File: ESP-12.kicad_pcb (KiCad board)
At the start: 2 copper layers, 27 x 38.2 mm, 23 parts, among them P1 VCC, P2 GPIO_1, P3 SPI, P4 GPIO_2, P5 GND, SW1 FLASH, SW2 RESET, U1 ESP-12E, U2 AP1117-33

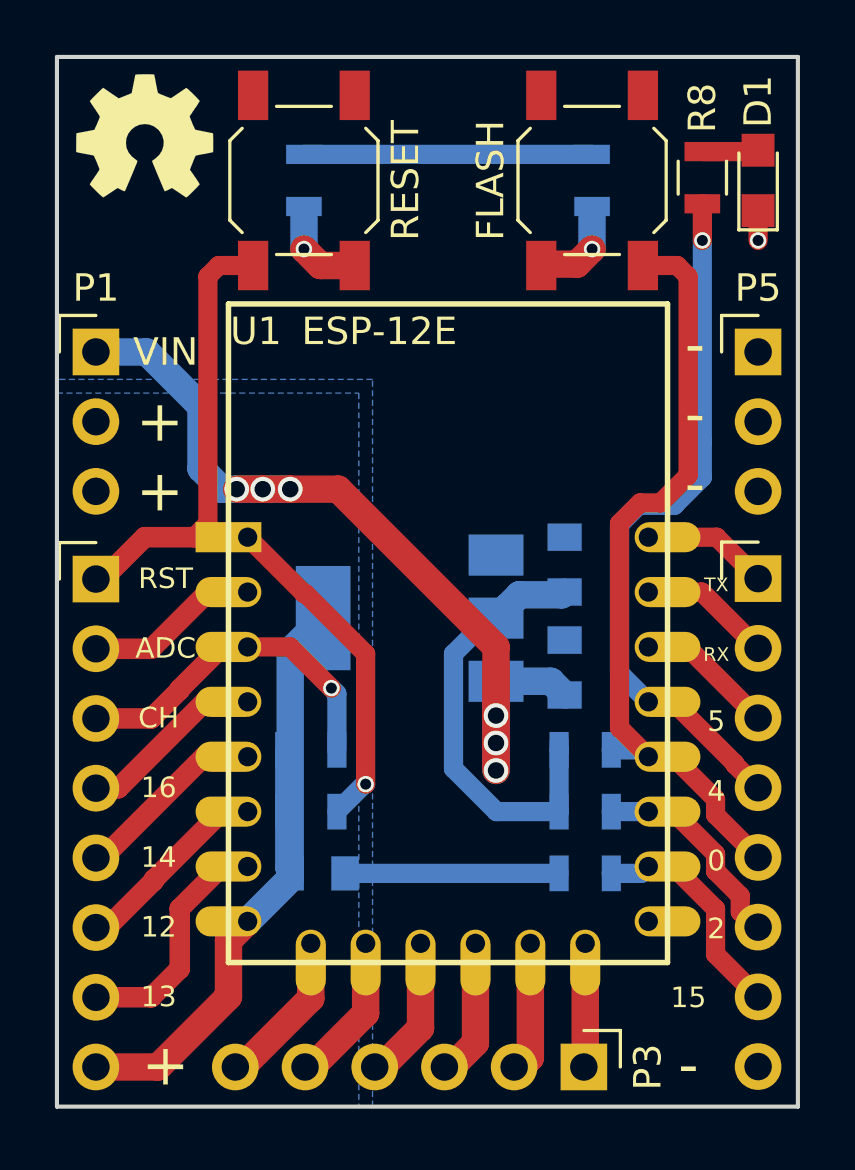
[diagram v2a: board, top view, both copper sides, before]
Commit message: Adjust pitch of power headers to match other headers
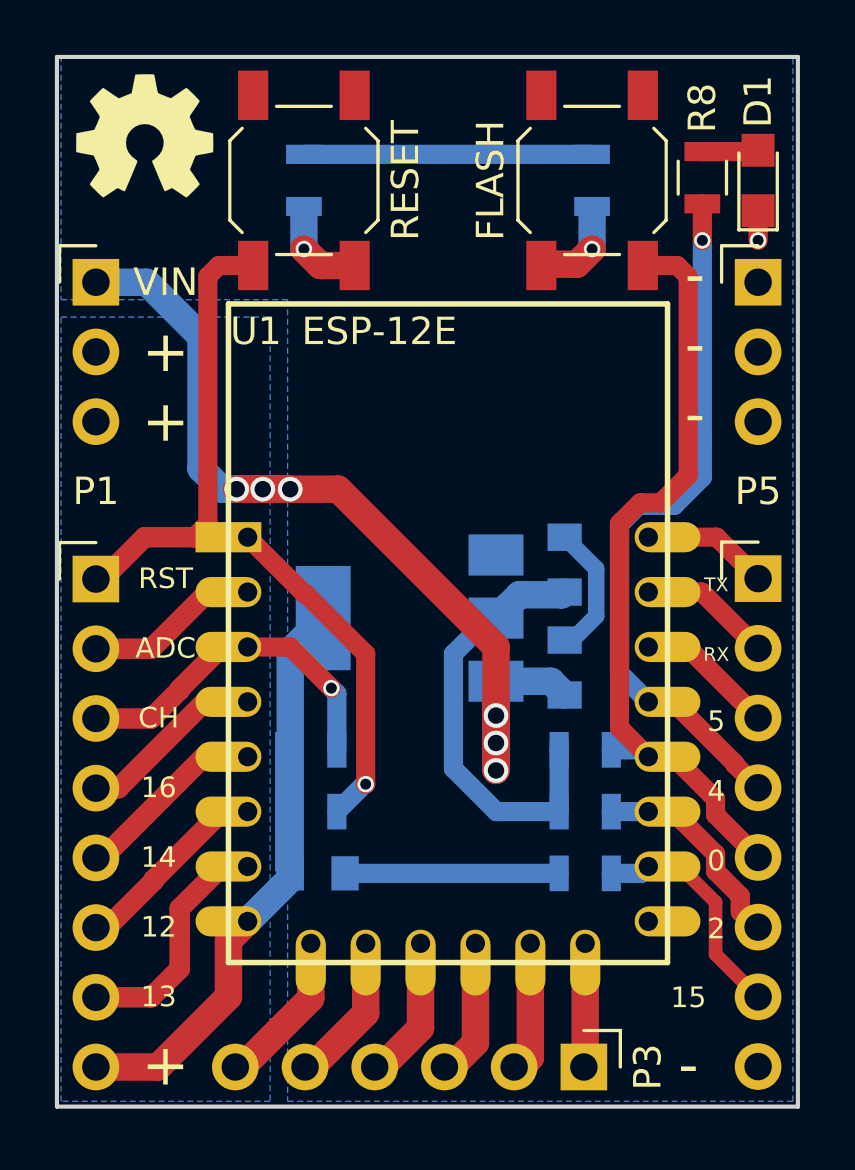
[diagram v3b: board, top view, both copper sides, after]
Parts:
- moved P1 2.54 mm to (27.4, 42.0)
- moved P5 2.54 mm to (51.5, 42.0)
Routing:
- net GND: track 19.6 -> 24.6 mm
- net /VIN: track 33.0 -> 35.3 mm
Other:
- board text added: "www.falseascension.xyz github.com/FalseAscension/"
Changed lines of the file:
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@@
   (general
     (links 60)
-    (no_connects 8)
-    (area 25.924999 33.674999 53.075001 72.075001)
+    (no_connects 7)
+    (area 14.150001 13.65 190.885715 164.950001)
     (thickness 1.6)
-    (drawings 61)
-    (tracks 162)
+    (drawings 62)
+    (tracks 168)
     (zones 0)
     (modules 23)
@@
   )
   (setup
-    (last_trace_width 0.7)
+    (last_trace_width 0.6)
     (user_trace_width 0.2)
     (user_trace_width 0.25)
@@
     (model /home/emil/Circuits/Library/kicad-ESP8266/ESP8266.3dshapes/ESP-12.wrl
       (at (xyz 0.025 0 0))
-      (scale (xyz 0.41 0.39 0.42))
+      (scale (xyz 0.41 0.395 0.42))
       (rotate (xyz 0 0 0))
     )
@@
   )
   (module Misc_Footprints:Pin_Header_Straight_1x03_Pitch2.54mm (layer F.Cu)
-    (at 51.55 44.5)
+    (at 51.55 41.96)
     (descr "Through hole straight pin header, 1x03, 2.54mm pitch, single row")
     (tags "Through hole pin header THT 1x03 2.54mm single row")
-    (fp_text reference P5 (at 0 -2.33) (layer F.SilkS)
-      (effects (font (size 1 1) (thickness 0.15)))
-    )
-    (fp_text value GND (at -0.05 -2.25) (layer F.Fab)
+    (fp_text reference P5 (at 0 7.62) (layer F.SilkS)
+      (effects (font (size 1 1) (thickness 0.15)))
+    )
+    (fp_text value GND (at 0 7.62) (layer F.Fab)
       (effects (font (size 1 1) (thickness 0.15)))
     )
@@
   )
   (module Misc_Footprints:Pin_Header_Straight_1x03_Pitch2.54mm (layer F.Cu)
-    (at 27.42 44.5)
+    (at 27.42 41.96)
     (descr "Through hole straight pin header, 1x03, 2.54mm pitch, single row")
     (tags "Through hole pin header THT 1x03 2.54mm single row")
-    (fp_text reference P1 (at 0 -2.33) (layer F.SilkS)
-      (effects (font (size 1 1) (thickness 0.15)))
-    )
-    (fp_text value VCC (at -0.05 -2.25) (layer F.Fab)
+    (fp_text reference P1 (at 0 7.62) (layer F.SilkS)
+      (effects (font (size 1 1) (thickness 0.15)))
+    )
+    (fp_text value VCC (at -0.05 7.62) (layer F.Fab)
       (effects (font (size 1 1) (thickness 0.15)))
     )
@@
       (effects (font (size 0.13462 0.13462) (thickness 0.0254)) (justify mirror))
     )
-    (fp_text user github.com/FalseAscension (at 7.578 -0.114 180) (layer B.SilkS)
+    (fp_text user github.com/FalseAscension (at 7.578 -0.114 180) (layer B.SilkS) hide
       (effects (font (size 0.8 0.8) (thickness 0.125)) (justify mirror))
     )
-    (fp_text user www.falseascension.xyz (at 7.324 1.156 180) (layer B.SilkS)
+    (fp_text user www.falseascension.xyz (at 7.324 1.156 180) (layer B.SilkS) hide
       (effects (font (size 1 1) (thickness 0.125)) (justify mirror))
     )
@@
       (xy -1.51384 2.24536)) (layer F.SilkS) (width 0.00254))
   )
+  (gr_text "www.falseascension.xyz\ngithub.com/FalseAscension/" (at 44.438 35.356) (layer B.SilkS)
+    (effects (font (size 0.75 0.75) (thickness 0.15)) (justify mirror))
+  )
   (gr_text "2\n\n\n" (at 50.026 66.725) (layer F.SilkS)
     (effects (font (size 0.75 0.75) (thickness 0.15)))
@@
     (effects (font (size 1.5 1.5) (thickness 0.3)) (justify mirror))
   )
-  (gr_text "12\n" (at 29.706 65.328 360) (layer B.SilkS)
+  (gr_text "12\n" (at 29.706 65.328) (layer B.SilkS)
     (effects (font (size 0.75 0.75) (thickness 0.15)) (justify mirror))
   )
-  (gr_text 14 (at 29.706 62.915 360) (layer B.SilkS)
+  (gr_text 14 (at 29.706 62.915) (layer B.SilkS)
     (effects (font (size 0.75 0.75) (thickness 0.15)) (justify mirror))
   )
-  (gr_text 16 (at 29.706 60.375 360) (layer B.SilkS)
+  (gr_text 16 (at 29.706 60.375) (layer B.SilkS)
     (effects (font (size 0.75 0.75) (thickness 0.15)) (justify mirror))
   )
-  (gr_text "CH\n" (at 29.706 57.962 360) (layer B.SilkS)
+  (gr_text "CH\n" (at 29.706 57.962) (layer B.SilkS)
     (effects (font (size 0.75 0.75) (thickness 0.15)) (justify mirror))
   )
-  (gr_text ADC (at 29.951708 55.295 360) (layer B.SilkS)
+  (gr_text ADC (at 29.951708 55.295) (layer B.SilkS)
     (effects (font (size 0.75 0.75) (thickness 0.15)) (justify mirror))
   )
-  (gr_text RST (at 29.951708 52.755 360) (layer B.SilkS)
+  (gr_text RST (at 29.951708 52.755) (layer B.SilkS)
     (effects (font (size 0.75 0.75) (thickness 0.15)) (justify mirror))
   )
-  (gr_text "13\n" (at 29.706 67.995 360) (layer B.SilkS)
+  (gr_text "13\n" (at 29.706 67.995) (layer B.SilkS)
     (effects (font (size 0.75 0.75) (thickness 0.15)) (justify mirror))
   )
@@
     (effects (font (size 1.5 1.5) (thickness 0.3)))
   )
-  (gr_text - (at 49.25 49.58 180) (layer F.SilkS)
+  (gr_text - (at 49.25 41.96 180) (layer F.SilkS)
     (effects (font (size 1.5 1.5) (thickness 0.3)))
   )
-  (gr_text "VIN\n" (at 29.96 44.5) (layer F.SilkS)
+  (gr_text "VIN\n" (at 29.96 41.96) (layer F.SilkS)
     (effects (font (size 1 1) (thickness 0.2)))
   )
-  (gr_text + (at 29.75 47.04) (layer F.SilkS)
+  (gr_text + (at 29.96 44.5) (layer F.SilkS)
     (effects (font (size 1.5 1.5) (thickness 0.3)))
   )
-  (gr_text + (at 29.75 49.58) (layer F.SilkS)
+  (gr_text + (at 29.96 47.04) (layer F.SilkS)
     (effects (font (size 1.5 1.5) (thickness 0.3)))
   )
@@
     (effects (font (size 1.5 1.5) (thickness 0.3)))
   )
+  (segment (start 44.5 51.25) (end 45.64998 52.39998) (width 0.6) (layer B.Cu) (net 1))
+  (segment (start 45.64998 52.39998) (end 45.64998 54.125022) (width 0.6) (layer B.Cu) (net 1))
+  (segment (start 45.64998 54.125022) (end 44.775002 55) (width 0.6) (layer B.Cu) (net 1))
+  (segment (start 44.775002 55) (end 44.5 55) (width 0.6) (layer B.Cu) (net 1))
+  (segment (start 44.5 55) (end 44.625 55) (width 0.25) (layer B.Cu) (net 1))
   (segment (start 45.5 37.3) (end 35 37.3) (width 0.7) (layer B.Cu) (net 1))
   (segment (start 51.55 39.35) (end 51.55 40.436) (width 0.7) (layer F.Cu) (net 1))
@@
   (segment (start 27.67 70.556) (end 29.686 70.556) (width 1) (layer F.Cu) (net 2))
   (segment (start 29.686 70.556) (end 32.25 67.992) (width 1) (layer F.Cu) (net 2))
+  (segment (start 27.42 44.5) (end 27.42 44.745998) (width 1) (layer B.Cu) (net 2))
   (segment (start 32.95 53.25) (end 31.502 53.25) (width 0.75) (layer F.Cu) (net 3))
   (segment (start 31.502 53.25) (end 29.436 55.316) (width 0.75) (layer F.Cu) (net 3))
@@
   (segment (start 35.25 66.25) (end 35.25 68.056) (width 1) (layer F.Cu) (net 19))
   (segment (start 35.25 68.056) (end 32.75 70.556) (width 1) (layer F.Cu) (net 19))
+  (segment (start 50 64.551375) (end 50 66.45) (width 0.5) (layer F.Cu) (net 20))
+  (segment (start 50 66.45) (end 51.55 68) (width 0.5) (layer F.Cu) (net 20))
+  (segment (start 47.55 63.25) (end 48.698625 63.25) (width 0.5) (layer F.Cu) (net 20))
+  (segment (start 48.698625 63.25) (end 50 64.551375) (width 0.5) (layer F.Cu) (net 20))
+  (segment (start 51.25 68) (end 51.55 68) (width 0.7) (layer F.Cu) (net 20))
   (segment (start 46.2 63.5) (end 47.3 63.5) (width 0.7) (layer B.Cu) (net 20))
   (segment (start 47.3 63.5) (end 47.55 63.25) (width 0.7) (layer B.Cu) (net 20))
-  (segment (start 50 66.45) (end 50 64.794351) (width 0.7) (layer F.Cu) (net 20))
-  (segment (start 48.455649 63.25) (end 47.55 63.25) (width 0.7) (layer F.Cu) (net 20))
-  (segment (start 50 64.794351) (end 48.455649 63.25) (width 0.7) (layer F.Cu) (net 20))
-  (segment (start 50 66.45) (end 51.55 68) (width 0.7) (layer F.Cu) (net 20))
   (segment (start 37.25 60.25) (end 37.2 60.25) (width 0.7) (layer B.Cu) (net 21))
   (segment (start 37.2 60.25) (end 36.2 61.25) (width 0.7) (layer B.Cu) (net 21))
@@
   (segment (start 32.008996 55.25) (end 32.95 55.25) (width 0.75) (layer F.Cu) (net 24))
   (segment (start 30.47499 56.784006) (end 32.008996 55.25) (width 0.75) (layer F.Cu) (net 24))
+  (segment (start 27.42 41.96) (end 29.27 41.96) (width 1) (layer B.Cu) (net 25))
+  (segment (start 29.27 41.96) (end 31.25 43.94) (width 1) (layer B.Cu) (net 25))
+  (segment (start 31.25 43.94) (end 31.25 48.75) (width 1) (layer B.Cu) (net 25))
+  (segment (start 31.25 48.75) (end 32 49.5) (width 1) (layer B.Cu) (net 25))
+  (segment (start 32 49.5) (end 32.55001 49.5) (width 1) (layer B.Cu) (net 25))
   (segment (start 42 56.5) (end 42 59.75) (width 1) (layer B.Cu) (net 25))
   (segment (start 42 58.75) (end 42 59.75) (width 1) (layer F.Cu) (net 25))
@@
   (via (at 33.5 49.5) (size 0.9) (drill 0.6) (layers F.Cu B.Cu) (net 25))
   (via (at 32.55001 49.5) (size 0.9) (drill 0.6) (layers F.Cu B.Cu) (net 25))
-  (segment (start 32.55001 49.5) (end 32 49.5) (width 1) (layer B.Cu) (net 25))
   (segment (start 42 55.25) (end 36.25 49.5) (width 1) (layer F.Cu) (net 25))
   (segment (start 42 57.75) (end 42 55.25) (width 1) (layer F.Cu) (net 25))
@@
   (via (at 42 58.75) (size 0.9) (drill 0.6) (layers F.Cu B.Cu) (net 25))
   (via (at 42 57.75) (size 0.9) (drill 0.6) (layers F.Cu B.Cu) (net 25))
-  (segment (start 29.27 44.5) (end 27.42 44.5) (width 1) (layer B.Cu) (net 25))
-  (segment (start 32 49.5) (end 31.25 48.75) (width 1) (layer B.Cu) (net 25))
-  (segment (start 31.25 48.75) (end 31.25 46.48) (width 1) (layer B.Cu) (net 25))
-  (segment (start 31.25 46.48) (end 29.27 44.5) (width 1) (layer B.Cu) (net 25))
-  (segment (start 27.42 44.5) (end 27.42 44.745998) (width 1) (layer B.Cu) (net 25))
   (segment (start 42 56.5) (end 44 56.5) (width 1) (layer B.Cu) (net 25))
   (segment (start 44 56.5) (end 44.5 57) (width 1) (layer B.Cu) (net 25))
@@
     (polygon
       (pts
-        (xy 26 72) (xy 26 46) (xy 37 46) (xy 37 72)
+        (xy 33.77 71.805) (xy 26.15 71.805) (xy 26.15 43.23) (xy 33.77 43.23)
       )
     )
@@
     (polygon
       (pts
-        (xy 37.5 72) (xy 37.5 45.5) (xy 26 45.5) (xy 26 33.75) (xy 53 33.75)
-        (xy 53 72)
+        (xy 26.15 42.595) (xy 34.405 42.595) (xy 34.405 71.805) (xy 52.82 71.805) (xy 52.82 33.705)
+        (xy 26.15 33.705)
       )
     )
